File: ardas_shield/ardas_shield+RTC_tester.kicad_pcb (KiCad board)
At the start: 2 copper layers, 92.8 x 56.3 mm, 66 parts, among them CON1 SD_Card, IC1 DS1307, P1 CONN_10, P1 I2C/SQW, P10 CONN_01X03, P2 CONN_8, P2 PWR, P3 CONN_8, P4 CONN_ICSP, P5 CONN_6, P6 TTL_COMM, P7 CONN_01X03, P8 CONN_01X03, P9 CONN_01X03, U1 74HC595, U2 74HC165, U3 SN74LV8154, U4 74HC165, U5 LD1117S33TR, U6 SN74LV8154, U7 74LVC1G125, U8 74LVC1G125, U9 74LVC1G125, X1 CRYSTAL

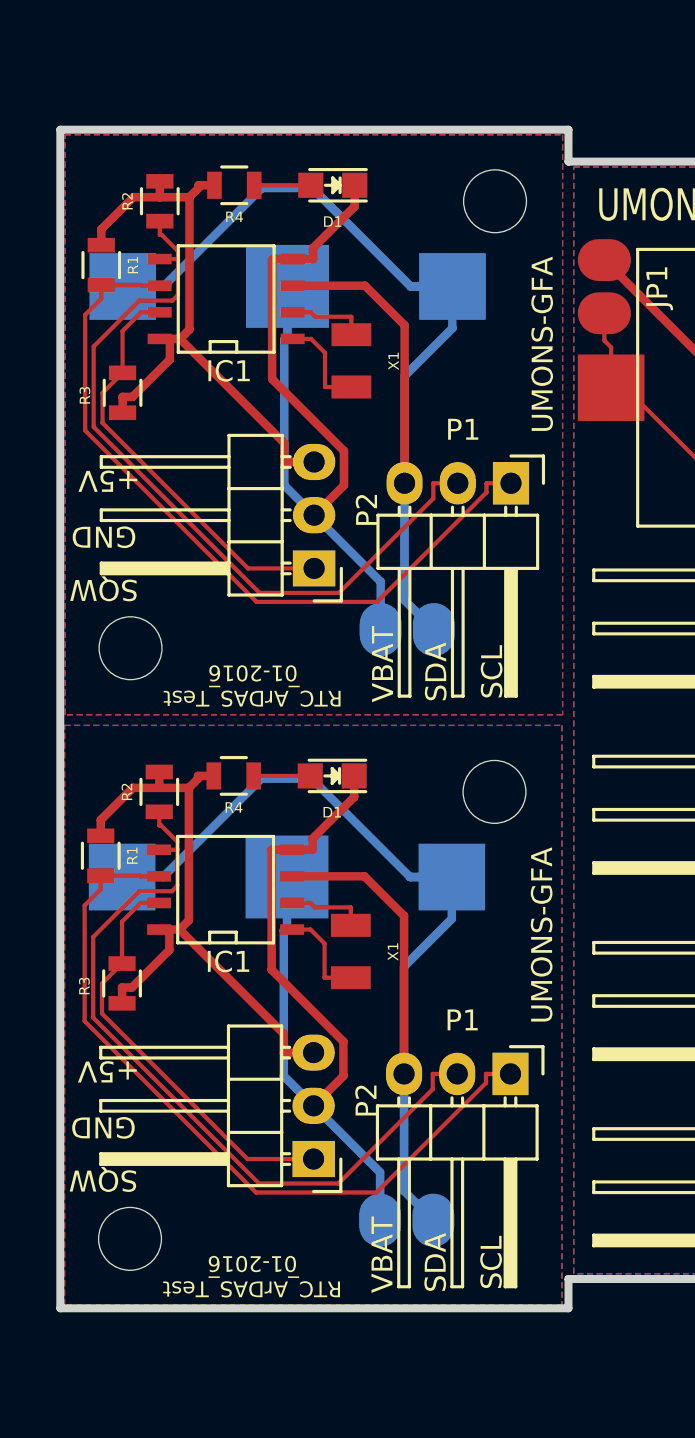
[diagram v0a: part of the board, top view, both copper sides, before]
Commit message: updated ardas_shield+RTC_tester.kicad_pcb
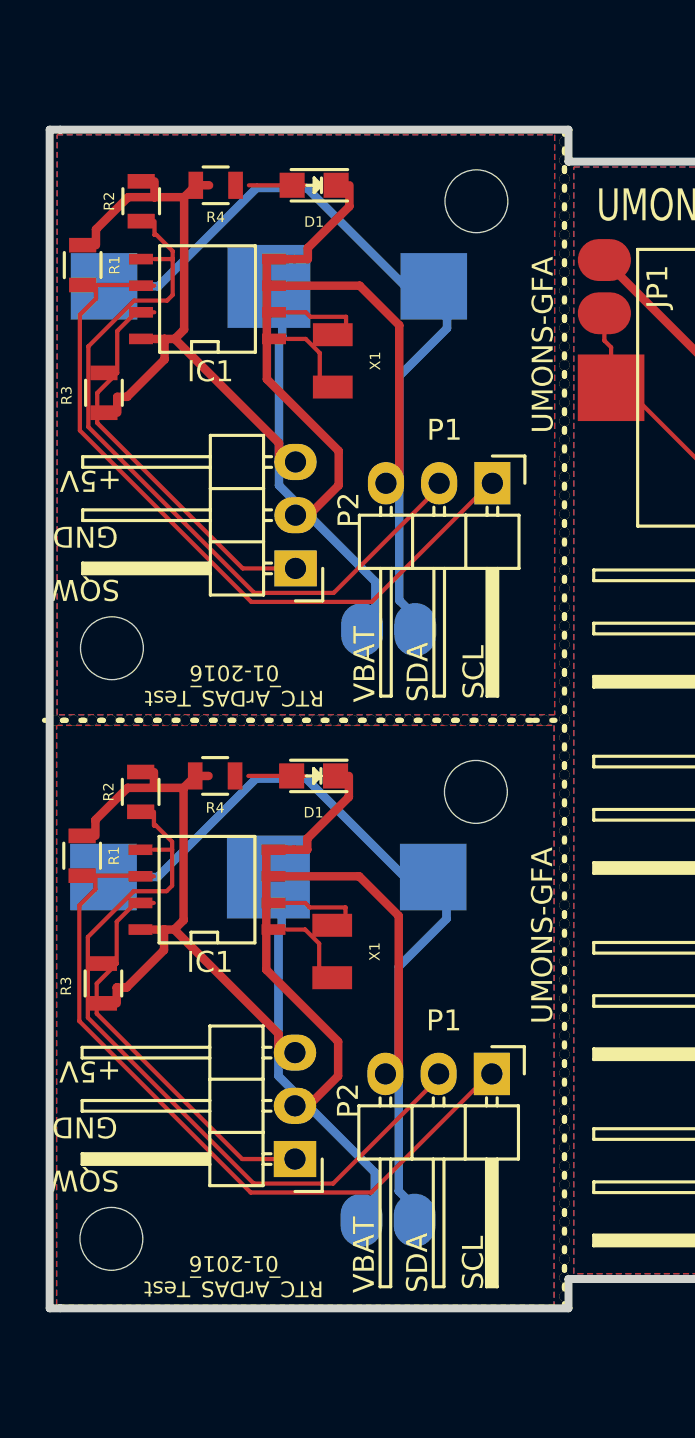
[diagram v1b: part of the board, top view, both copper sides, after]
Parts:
- removed the BT1 at (33.6, 74.1)
- removed the BT1 at (33.6, 102.3)
- removed the D1 at (35.8, 69.3)
- removed the D1 at (35.8, 97.5)
- removed the IC1 at (30.7, 74.7)
- removed the IC1 at (30.7, 102.9)
- removed the JP1 at (39.4, 90.5)
- removed the JP1 at (39.3, 118.7)
- removed the MH2 at (43.5, 70.1)
- removed the MH2 at (43.5, 98.3)
- removed the MH3 at (26.1, 91.4)
- removed the MH3 at (26.1, 119.6)
- removed the P1 at (44.3, 83.5)
- removed the P1 at (44.3, 111.7)
- removed the P2 at (34.9, 87.6)
- removed the P2 at (34.9, 115.8)
- removed the R1 at (24.8, 73.1)
- removed the R1 at (24.7, 101.3)
- removed the R2 at (27.5, 70.1)
- removed the R2 at (27.5, 98.3)
- removed the R3 at (25.8, 79.2)
- removed the R3 at (25.7, 107.4)
- removed the R4 at (31.1, 69.3)
- removed the R4 at (31.1, 97.5)
- removed the X1 at (36.7, 77.7)
- removed the X1 at (36.7, 105.9)
- added BT1: Battery, MyFootprints:BATTERY_KEYSTONE_12mm, B.Cu at (32.8, 74.1)
- added BT1: Battery, MyFootprints:BATTERY_KEYSTONE_12mm, B.Cu at (32.7, 102.3)
- added CH: CuttingHole_0.5mm, kicad-gfa local:CuttingHole_0.5mm, F.Cu at (46.9, 78.8)
- added CH: CuttingHole_0.5mm, kicad-gfa local:CuttingHole_0.5mm, F.Cu at (46.9, 84.1)
- added CH: CuttingHole_0.5mm, kicad-gfa local:CuttingHole_0.5mm, F.Cu at (46.9, 86.8)
- added CH: CuttingHole_0.5mm, kicad-gfa local:CuttingHole_0.5mm, F.Cu at (46.9, 87.7)
- added CH: CuttingHole_0.5mm, kicad-gfa local:CuttingHole_0.5mm, F.Cu at (46.9, 88.6)
- added CH: CuttingHole_0.5mm, kicad-gfa local:CuttingHole_0.5mm, F.Cu at (46.9, 77.9)
- added CH: CuttingHole_0.5mm, kicad-gfa local:CuttingHole_0.5mm, F.Cu at (46.9, 77.0)
- added CH: CuttingHole_0.5mm, kicad-gfa local:CuttingHole_0.5mm, F.Cu at (46.9, 76.1)
- added CH: CuttingHole_0.5mm, kicad-gfa local:CuttingHole_0.5mm, F.Cu at (46.9, 73.5)
- added CH: CuttingHole_0.5mm, kicad-gfa local:CuttingHole_0.5mm, F.Cu at (46.9, 74.3)
- added CH: CuttingHole_0.5mm, kicad-gfa local:CuttingHole_0.5mm, F.Cu at (46.9, 75.2)
- added CH: CuttingHole_0.5mm, kicad-gfa local:CuttingHole_0.5mm, F.Cu at (46.9, 93.9)
- added CH: CuttingHole_0.5mm, kicad-gfa local:CuttingHole_0.5mm, F.Cu at (46.9, 80.6)
- added CH: CuttingHole_0.5mm, kicad-gfa local:CuttingHole_0.5mm, F.Cu at (46.9, 79.7)
- added CH: CuttingHole_0.5mm, kicad-gfa local:CuttingHole_0.5mm, F.Cu at (46.9, 81.5)
- added CH: CuttingHole_0.5mm, kicad-gfa local:CuttingHole_0.5mm, F.Cu at (46.9, 82.3)
- added CH: CuttingHole_0.5mm, kicad-gfa local:CuttingHole_0.5mm, F.Cu at (46.9, 83.2)
- added CH: CuttingHole_0.5mm, kicad-gfa local:CuttingHole_0.5mm, F.Cu at (46.9, 72.6)
- added CH: CuttingHole_0.5mm, kicad-gfa local:CuttingHole_0.5mm, F.Cu at (46.9, 71.7)
- added CH: CuttingHole_0.5mm, kicad-gfa local:CuttingHole_0.5mm, F.Cu at (46.9, 70.8)
- added CH: CuttingHole_0.5mm, kicad-gfa local:CuttingHole_0.5mm, F.Cu at (46.9, 102.8)
- added CH: CuttingHole_0.5mm, kicad-gfa local:CuttingHole_0.5mm, F.Cu at (46.9, 117.9)
- added CH: CuttingHole_0.5mm, kicad-gfa local:CuttingHole_0.5mm, F.Cu at (46.9, 93.0)
- added CH: CuttingHole_0.5mm, kicad-gfa local:CuttingHole_0.5mm, F.Cu at (46.9, 117.0)
- added CH: CuttingHole_0.5mm, kicad-gfa local:CuttingHole_0.5mm, F.Cu at (46.9, 116.1)
- added CH: CuttingHole_0.5mm, kicad-gfa local:CuttingHole_0.5mm, F.Cu at (46.9, 113.5)
- added CH: CuttingHole_0.5mm, kicad-gfa local:CuttingHole_0.5mm, F.Cu at (46.9, 114.4)
- added CH: CuttingHole_0.5mm, kicad-gfa local:CuttingHole_0.5mm, F.Cu at (46.9, 115.2)
- added CH: CuttingHole_0.5mm, kicad-gfa local:CuttingHole_0.5mm, F.Cu at (46.9, 109.9)
- added CH: CuttingHole_0.5mm, kicad-gfa local:CuttingHole_0.5mm, F.Cu at (46.9, 109.0)
- added CH: CuttingHole_0.5mm, kicad-gfa local:CuttingHole_0.5mm, F.Cu at (46.9, 108.1)
- added CH: CuttingHole_0.5mm, kicad-gfa local:CuttingHole_0.5mm, F.Cu at (46.9, 110.8)
- added CH: CuttingHole_0.5mm, kicad-gfa local:CuttingHole_0.5mm, F.Cu at (46.9, 111.7)
- added CH: CuttingHole_0.5mm, kicad-gfa local:CuttingHole_0.5mm, F.Cu at (46.9, 92.1)
- added CH: CuttingHole_0.5mm, kicad-gfa local:CuttingHole_0.5mm, F.Cu at (46.9, 112.6)
- added CH: CuttingHole_0.5mm, kicad-gfa local:CuttingHole_0.5mm, F.Cu at (46.9, 101.9)
- added CH: CuttingHole_0.5mm, kicad-gfa local:CuttingHole_0.5mm, F.Cu at (46.9, 101.0)
- added CH: CuttingHole_0.5mm, kicad-gfa local:CuttingHole_0.5mm, F.Cu at (46.9, 100.1)
- added CH: CuttingHole_0.5mm, kicad-gfa local:CuttingHole_0.5mm, F.Cu at (46.9, 97.5)
- added CH: CuttingHole_0.5mm, kicad-gfa local:CuttingHole_0.5mm, F.Cu at (46.9, 98.3)
- added CH: CuttingHole_0.5mm, kicad-gfa local:CuttingHole_0.5mm, F.Cu at (46.9, 99.2)
- added CH: CuttingHole_0.5mm, kicad-gfa local:CuttingHole_0.5mm, F.Cu at (46.9, 104.6)
- added CH: CuttingHole_0.5mm, kicad-gfa local:CuttingHole_0.5mm, F.Cu at (46.9, 103.7)
- added CH: CuttingHole_0.5mm, kicad-gfa local:CuttingHole_0.5mm, F.Cu at (46.9, 105.5)
- added CH: CuttingHole_0.5mm, kicad-gfa local:CuttingHole_0.5mm, F.Cu at (46.9, 89.5)
- added CH: CuttingHole_0.5mm, kicad-gfa local:CuttingHole_0.5mm, F.Cu at (46.9, 106.3)
- added CH: CuttingHole_0.5mm, kicad-gfa local:CuttingHole_0.5mm, F.Cu at (46.9, 107.2)
- added CH: CuttingHole_0.5mm, kicad-gfa local:CuttingHole_0.5mm, F.Cu at (46.9, 96.6)
- added CH: CuttingHole_0.5mm, kicad-gfa local:CuttingHole_0.5mm, F.Cu at (46.9, 95.7)
- added CH: CuttingHole_0.5mm, kicad-gfa local:CuttingHole_0.5mm, F.Cu at (46.9, 94.8)
- added CH: CuttingHole_0.5mm, kicad-gfa local:CuttingHole_0.5mm, F.Cu at (46.9, 118.8)
- added CH: CuttingHole_0.5mm, kicad-gfa local:CuttingHole_0.5mm, F.Cu at (46.9, 119.7)
- added CH: CuttingHole_0.5mm, kicad-gfa local:CuttingHole_0.5mm, F.Cu at (46.9, 120.6)
- added CH: CuttingHole_0.5mm, kicad-gfa local:CuttingHole_0.5mm, F.Cu at (46.9, 122.4)
- added CH: CuttingHole_0.5mm, kicad-gfa local:CuttingHole_0.5mm, F.Cu at (46.9, 121.5)
- added CH: CuttingHole_0.5mm, kicad-gfa local:CuttingHole_0.5mm, F.Cu at (46.9, 90.3)
- added CH: CuttingHole_0.5mm, kicad-gfa local:CuttingHole_0.5mm, F.Cu at (46.9, 67.2)
- added CH: CuttingHole_0.5mm, kicad-gfa local:CuttingHole_0.5mm, F.Cu at (46.9, 68.1)
- added CH: CuttingHole_0.5mm, kicad-gfa local:CuttingHole_0.5mm, F.Cu at (46.9, 69.0)
- added CH: CuttingHole_0.5mm, kicad-gfa local:CuttingHole_0.5mm, F.Cu at (46.9, 69.9)
- added CH: CuttingHole_0.5mm, kicad-gfa local:CuttingHole_0.5mm, F.Cu at (37.7, 94.9)
- added CH: CuttingHole_0.5mm, kicad-gfa local:CuttingHole_0.5mm, F.Cu at (22.5, 94.9)
- added CH: CuttingHole_0.5mm, kicad-gfa local:CuttingHole_0.5mm, F.Cu at (23.4, 94.9)
- added CH: CuttingHole_0.5mm, kicad-gfa local:CuttingHole_0.5mm, F.Cu at (24.3, 94.9)
- added CH: CuttingHole_0.5mm, kicad-gfa local:CuttingHole_0.5mm, F.Cu at (27.0, 94.9)
- added CH: CuttingHole_0.5mm, kicad-gfa local:CuttingHole_0.5mm, F.Cu at (26.1, 94.9)
- added CH: CuttingHole_0.5mm, kicad-gfa local:CuttingHole_0.5mm, F.Cu at (46.9, 91.2)
- added CH: CuttingHole_0.5mm, kicad-gfa local:CuttingHole_0.5mm, F.Cu at (25.2, 94.9)
- added CH: CuttingHole_0.5mm, kicad-gfa local:CuttingHole_0.5mm, F.Cu at (30.5, 94.9)
- added CH: CuttingHole_0.5mm, kicad-gfa local:CuttingHole_0.5mm, F.Cu at (31.4, 94.9)
- added CH: CuttingHole_0.5mm, kicad-gfa local:CuttingHole_0.5mm, F.Cu at (32.3, 94.9)
- added CH: CuttingHole_0.5mm, kicad-gfa local:CuttingHole_0.5mm, F.Cu at (29.7, 94.9)
- added CH: CuttingHole_0.5mm, kicad-gfa local:CuttingHole_0.5mm, F.Cu at (28.8, 94.9)
- added CH: CuttingHole_0.5mm, kicad-gfa local:CuttingHole_0.5mm, F.Cu at (27.9, 94.9)
- added CH: CuttingHole_0.5mm, kicad-gfa local:CuttingHole_0.5mm, F.Cu at (38.5, 94.9)
- added CH: CuttingHole_0.5mm, kicad-gfa local:CuttingHole_0.5mm, F.Cu at (39.4, 94.9)
- added CH: CuttingHole_0.5mm, kicad-gfa local:CuttingHole_0.5mm, F.Cu at (40.3, 94.9)
- added CH: CuttingHole_0.5mm, kicad-gfa local:CuttingHole_0.5mm, F.Cu at (46.9, 85.9)
- added CH: CuttingHole_0.5mm, kicad-gfa local:CuttingHole_0.5mm, F.Cu at (43.0, 94.9)
- added CH: CuttingHole_0.5mm, kicad-gfa local:CuttingHole_0.5mm, F.Cu at (42.1, 94.9)
- added CH: CuttingHole_0.5mm, kicad-gfa local:CuttingHole_0.5mm, F.Cu at (41.2, 94.9)
- added CH: CuttingHole_0.5mm, kicad-gfa local:CuttingHole_0.5mm, F.Cu at (35.9, 94.9)
- added CH: CuttingHole_0.5mm, kicad-gfa local:CuttingHole_0.5mm, F.Cu at (36.8, 94.9)
- added CH: CuttingHole_0.5mm, kicad-gfa local:CuttingHole_0.5mm, F.Cu at (35.0, 94.9)
- added CH: CuttingHole_0.5mm, kicad-gfa local:CuttingHole_0.5mm, F.Cu at (34.1, 94.9)
- added CH: CuttingHole_0.5mm, kicad-gfa local:CuttingHole_0.5mm, F.Cu at (33.2, 94.9)
- added CH: CuttingHole_0.5mm, kicad-gfa local:CuttingHole_0.5mm, F.Cu at (43.9, 94.9)
- added CH: CuttingHole_0.5mm, kicad-gfa local:CuttingHole_0.5mm, F.Cu at (44.8, 94.9)
- added CH: CuttingHole_0.5mm, kicad-gfa local:CuttingHole_0.5mm, F.Cu at (46.9, 85.0)
- added CH: CuttingHole_0.5mm, kicad-gfa local:CuttingHole_0.5mm, F.Cu at (45.9, 94.9)
- added D1: Led_Small, LEDs:LED-0805, F.Cu at (34.9, 69.3)
- added D1: Led_Small, LEDs:LED-0805, F.Cu at (34.9, 97.5)
- added IC1: DS1307, SMD_Packages:SOIC-8-N, F.Cu at (29.8, 74.7)
- added IC1: DS1307, SMD_Packages:SOIC-8-N, F.Cu at (29.8, 102.9)
- added JP1: Jumper_NO_Small, MyFootprints:small_no_jumper, B.Cu at (38.5, 90.5)
- added JP1: Jumper_NO_Small, MyFootprints:small_no_jumper, B.Cu at (38.4, 118.7)
- added MH2: MountingHole_3mm, Mounting_Holes:MountingHole_3mm, F.Cu at (42.7, 70.1)
- added MH2: MountingHole_3mm, Mounting_Holes:MountingHole_3mm, F.Cu at (42.6, 98.3)
- added MH3: MountingHole_3mm, Mounting_Holes:MountingHole_3mm, F.Cu at (25.3, 91.4)
- added MH3: MountingHole_3mm, Mounting_Holes:MountingHole_3mm, F.Cu at (25.2, 119.6)
- added P1: I2C/SQW, Pin_Headers:Pin_Header_Angled_1x03, F.Cu at (43.4, 83.5)
- added P1: I2C/SQW, Pin_Headers:Pin_Header_Angled_1x03, F.Cu at (43.4, 111.7)
- added P2: PWR, Pin_Headers:Pin_Header_Angled_1x03, F.Cu at (34.0, 87.6)
- added P2: PWR, Pin_Headers:Pin_Header_Angled_1x03, F.Cu at (34.0, 115.8)
- added R1: 4.7K, Resistors_SMD:R_0805, F.Cu at (23.9, 73.1)
- added R1: 4.7K, Resistors_SMD:R_0805, F.Cu at (23.8, 101.3)
- added R2: 4.7K, Resistors_SMD:R_0805, F.Cu at (26.7, 70.1)
- added R2: 4.7K, Resistors_SMD:R_0805, F.Cu at (26.6, 98.3)
- added R3: 10K, Resistors_SMD:R_0805, F.Cu at (24.9, 79.2)
- added R3: 10K, Resistors_SMD:R_0805, F.Cu at (24.9, 107.4)
- added R4: 150, Resistors_SMD:R_0805, F.Cu at (30.2, 69.3)
- added R4: 150, Resistors_SMD:R_0805, F.Cu at (30.2, 97.5)
- added X1: CRYSTAL, MyFootprints:XTAL_ABRACON_ABS07, F.Cu at (35.8, 77.7)
- added X1: CRYSTAL, MyFootprints:XTAL_ABRACON_ABS07, F.Cu at (35.8, 105.9)
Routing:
- net (no net): track 0.00 -> 5.40 mm
- net Net-(D1-Pad2): track 5.40 -> 0.00 mm
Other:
- board size 92.8 x 56.3 mm -> 93.3 x 56.3 mm
- board text removed: "V-Scoring on back : 0.5mm 60°"
- board text removed: "V-Scoring on front : 0.5mm 60°"
